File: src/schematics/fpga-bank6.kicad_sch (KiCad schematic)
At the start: 7 parts

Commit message: Updates the root page
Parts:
- renumbered C72 to C66, C73 to C67, C74 to C68, C75 to C69, C76 to C70, C77 to C71
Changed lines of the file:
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@@
 		(dnp no)
 		(fields_autoplaced yes)
-		(property "Reference" "#PWR057"
+		(property "Reference" "#PWR050"
 			(at 148.59 45.72 0)
 			(effects
@@
 		(instances
 			(project "ecap5-bsom"
-				(path "/c5fd18a3-9aa0-4151-b6e0-94da3d606686/9ec64d27-698a-408d-bb9c-7e381193a80d/95fcda06-cda0-4eca-ae7c-fe055bbdf4e0"
-					(reference "#PWR057")
+				(path "/c5fd18a3-9aa0-4151-b6e0-94da3d606686/624c8ae5-3519-4938-8e49-46a13f6c30b9"
+					(reference "#PWR050")
 					(unit 1)
 				)
@@
 		(dnp no)
 		(fields_autoplaced yes)
-		(property "Reference" "#PWR054"
+		(property "Reference" "#PWR047"
 			(at 118.11 45.72 0)
 			(effects
@@
 		(instances
 			(project "ecap5-bsom"
-				(path "/c5fd18a3-9aa0-4151-b6e0-94da3d606686/9ec64d27-698a-408d-bb9c-7e381193a80d/95fcda06-cda0-4eca-ae7c-fe055bbdf4e0"
-					(reference "#PWR054")
+				(path "/c5fd18a3-9aa0-4151-b6e0-94da3d606686/624c8ae5-3519-4938-8e49-46a13f6c30b9"
+					(reference "#PWR047")
 					(unit 1)
 				)
@@
 		(dnp no)
 		(fields_autoplaced yes)
-		(property "Reference" "C75"
+		(property "Reference" "C69"
 			(at 146.05 34.2962 0)
 			(effects
@@
 		(instances
 			(project "ecap5-bsom"
-				(path "/c5fd18a3-9aa0-4151-b6e0-94da3d606686/9ec64d27-698a-408d-bb9c-7e381193a80d/95fcda06-cda0-4eca-ae7c-fe055bbdf4e0"
-					(reference "C75")
+				(path "/c5fd18a3-9aa0-4151-b6e0-94da3d606686/624c8ae5-3519-4938-8e49-46a13f6c30b9"
+					(reference "C69")
 					(unit 1)
 				)
@@
 		(dnp no)
 		(fields_autoplaced yes)
-		(property "Reference" "#PWR053"
+		(property "Reference" "#PWR046"
 			(at 118.11 31.75 0)
 			(effects
@@
 		(instances
 			(project "ecap5-bsom"
-				(path "/c5fd18a3-9aa0-4151-b6e0-94da3d606686/9ec64d27-698a-408d-bb9c-7e381193a80d/95fcda06-cda0-4eca-ae7c-fe055bbdf4e0"
-					(reference "#PWR053")
+				(path "/c5fd18a3-9aa0-4151-b6e0-94da3d606686/624c8ae5-3519-4938-8e49-46a13f6c30b9"
+					(reference "#PWR046")
 					(unit 1)
 				)
@@
 		(dnp no)
 		(fields_autoplaced yes)
-		(property "Reference" "#PWR059"
+		(property "Reference" "#PWR052"
 			(at 170.18 45.72 0)
 			(effects
@@
 		(instances
 			(project "ecap5-bsom"
-				(path "/c5fd18a3-9aa0-4151-b6e0-94da3d606686/9ec64d27-698a-408d-bb9c-7e381193a80d/95fcda06-cda0-4eca-ae7c-fe055bbdf4e0"
-					(reference "#PWR059")
+				(path "/c5fd18a3-9aa0-4151-b6e0-94da3d606686/624c8ae5-3519-4938-8e49-46a13f6c30b9"
+					(reference "#PWR052")
 					(unit 1)
 				)
@@
 		(dnp no)
 		(fields_autoplaced yes)
-		(property "Reference" "#PWR058"
+		(property "Reference" "#PWR051"
 			(at 158.75 45.72 0)
 			(effects
@@
 		(instances
 			(project "ecap5-bsom"
-				(path "/c5fd18a3-9aa0-4151-b6e0-94da3d606686/9ec64d27-698a-408d-bb9c-7e381193a80d/95fcda06-cda0-4eca-ae7c-fe055bbdf4e0"
-					(reference "#PWR058")
+				(path "/c5fd18a3-9aa0-4151-b6e0-94da3d606686/624c8ae5-3519-4938-8e49-46a13f6c30b9"
+					(reference "#PWR051")
 					(unit 1)
 				)
@@
 		(dnp no)
 		(fields_autoplaced yes)
-		(property "Reference" "#PWR055"
+		(property "Reference" "#PWR048"
 			(at 128.27 45.72 0)
 			(effects
@@
 		(instances
 			(project "ecap5-bsom"
-				(path "/c5fd18a3-9aa0-4151-b6e0-94da3d606686/9ec64d27-698a-408d-bb9c-7e381193a80d/95fcda06-cda0-4eca-ae7c-fe055bbdf4e0"
-					(reference "#PWR055")
+				(path "/c5fd18a3-9aa0-4151-b6e0-94da3d606686/624c8ae5-3519-4938-8e49-46a13f6c30b9"
+					(reference "#PWR048")
 					(unit 1)
 				)
@@
 		(dnp no)
 		(fields_autoplaced yes)
-		(property "Reference" "C72"
+		(property "Reference" "C66"
 			(at 115.57 34.2962 0)
 			(effects
@@
 		(instances
 			(project "ecap5-bsom"
-				(path "/c5fd18a3-9aa0-4151-b6e0-94da3d606686/9ec64d27-698a-408d-bb9c-7e381193a80d/95fcda06-cda0-4eca-ae7c-fe055bbdf4e0"
-					(reference "C72")
+				(path "/c5fd18a3-9aa0-4151-b6e0-94da3d606686/624c8ae5-3519-4938-8e49-46a13f6c30b9"
+					(reference "C66")
 					(unit 1)
 				)
@@
 		(dnp no)
 		(fields_autoplaced yes)
-		(property "Reference" "C73"
+		(property "Reference" "C67"
 			(at 125.73 34.2962 0)
 			(effects
@@
 		(instances
 			(project "ecap5-bsom"
-				(path "/c5fd18a3-9aa0-4151-b6e0-94da3d606686/9ec64d27-698a-408d-bb9c-7e381193a80d/95fcda06-cda0-4eca-ae7c-fe055bbdf4e0"
-					(reference "C73")
+				(path "/c5fd18a3-9aa0-4151-b6e0-94da3d606686/624c8ae5-3519-4938-8e49-46a13f6c30b9"
+					(reference "C67")
 					(unit 1)
 				)
@@
 		(dnp no)
 		(fields_autoplaced yes)
-		(property "Reference" "C76"
+		(property "Reference" "C70"
 			(at 156.21 34.2962 0)
 			(effects
@@
 		(instances
 			(project "ecap5-bsom"
-				(path "/c5fd18a3-9aa0-4151-b6e0-94da3d606686/9ec64d27-698a-408d-bb9c-7e381193a80d/95fcda06-cda0-4eca-ae7c-fe055bbdf4e0"
-					(reference "C76")
+				(path "/c5fd18a3-9aa0-4151-b6e0-94da3d606686/624c8ae5-3519-4938-8e49-46a13f6c30b9"
+					(reference "C70")
 					(unit 1)
 				)
@@
 		(dnp no)
 		(fields_autoplaced yes)
-		(property "Reference" "C74"
+		(property "Reference" "C68"
 			(at 135.89 34.2962 0)
 			(effects
@@
 		(instances
 			(project "ecap5-bsom"
-				(path "/c5fd18a3-9aa0-4151-b6e0-94da3d606686/9ec64d27-698a-408d-bb9c-7e381193a80d/95fcda06-cda0-4eca-ae7c-fe055bbdf4e0"
-					(reference "C74")
+				(path "/c5fd18a3-9aa0-4151-b6e0-94da3d606686/624c8ae5-3519-4938-8e49-46a13f6c30b9"
+					(reference "C68")
 					(unit 1)
 				)
@@
 		(dnp no)
 		(fields_autoplaced yes)
-		(property "Reference" "#PWR056"
+		(property "Reference" "#PWR049"
 			(at 138.43 45.72 0)
 			(effects
@@
 		(instances
 			(project "ecap5-bsom"
-				(path "/c5fd18a3-9aa0-4151-b6e0-94da3d606686/9ec64d27-698a-408d-bb9c-7e381193a80d/95fcda06-cda0-4eca-ae7c-fe055bbdf4e0"
-					(reference "#PWR056")
+				(path "/c5fd18a3-9aa0-4151-b6e0-94da3d606686/624c8ae5-3519-4938-8e49-46a13f6c30b9"
+					(reference "#PWR049")
 					(unit 1)
 				)
@@
 		(dnp no)
 		(fields_autoplaced yes)
-		(property "Reference" "C77"
+		(property "Reference" "C71"
 			(at 167.64 34.2962 0)
 			(effects
@@
 		(instances
 			(project "ecap5-bsom"
-				(path "/c5fd18a3-9aa0-4151-b6e0-94da3d606686/9ec64d27-698a-408d-bb9c-7e381193a80d/95fcda06-cda0-4eca-ae7c-fe055bbdf4e0"
-					(reference "C77")
+				(path "/c5fd18a3-9aa0-4151-b6e0-94da3d606686/624c8ae5-3519-4938-8e49-46a13f6c30b9"
+					(reference "C71")
 					(unit 1)
 				)
@@
 		(instances
 			(project "ecap5-bsom"
-				(path "/c5fd18a3-9aa0-4151-b6e0-94da3d606686/9ec64d27-698a-408d-bb9c-7e381193a80d/95fcda06-cda0-4eca-ae7c-fe055bbdf4e0"
+				(path "/c5fd18a3-9aa0-4151-b6e0-94da3d606686/624c8ae5-3519-4938-8e49-46a13f6c30b9"
 					(reference "U6")
 					(unit 7)

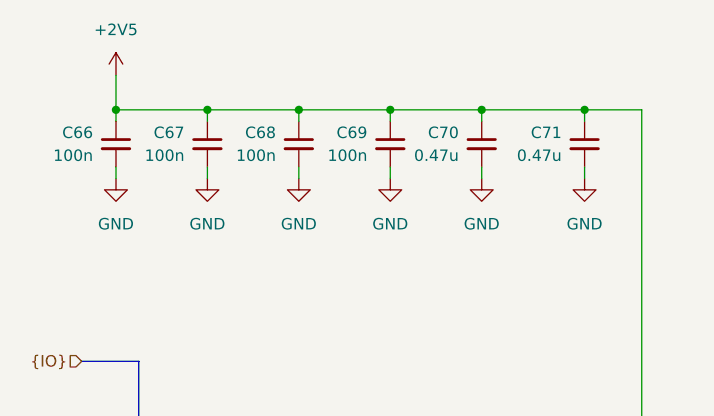
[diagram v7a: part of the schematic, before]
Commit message: Fixes ERC issues
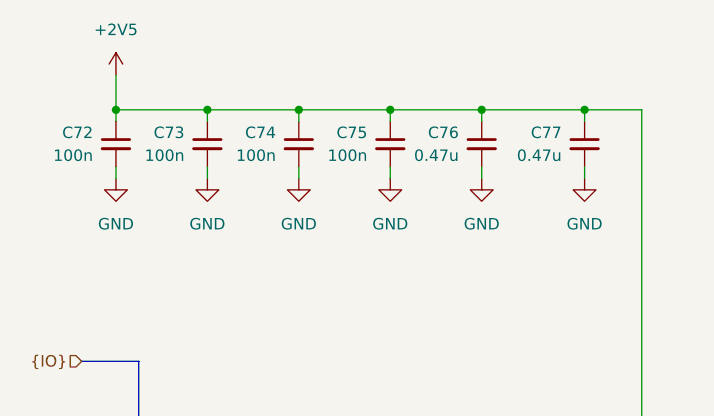
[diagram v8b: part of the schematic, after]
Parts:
- renumbered C66 to C72, C67 to C73, C68 to C74, C69 to C75, C70 to C76, C71 to C77
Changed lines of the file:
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@@
 		(dnp no)
 		(fields_autoplaced yes)
-		(property "Reference" "#PWR050"
+		(property "Reference" "#PWR058"
 			(at 148.59 45.72 0)
 			(effects
@@
 			(project "ecap5-bsom"
 				(path "/c5fd18a3-9aa0-4151-b6e0-94da3d606686/624c8ae5-3519-4938-8e49-46a13f6c30b9"
-					(reference "#PWR050")
+					(reference "#PWR058")
 					(unit 1)
 				)
@@
 		(dnp no)
 		(fields_autoplaced yes)
-		(property "Reference" "#PWR047"
+		(property "Reference" "#PWR055"
 			(at 118.11 45.72 0)
 			(effects
@@
 			(project "ecap5-bsom"
 				(path "/c5fd18a3-9aa0-4151-b6e0-94da3d606686/624c8ae5-3519-4938-8e49-46a13f6c30b9"
-					(reference "#PWR047")
+					(reference "#PWR055")
 					(unit 1)
 				)
@@
 		(dnp no)
 		(fields_autoplaced yes)
-		(property "Reference" "C69"
+		(property "Reference" "C75"
 			(at 146.05 34.2962 0)
 			(effects
@@
 			(project "ecap5-bsom"
 				(path "/c5fd18a3-9aa0-4151-b6e0-94da3d606686/624c8ae5-3519-4938-8e49-46a13f6c30b9"
-					(reference "C69")
+					(reference "C75")
 					(unit 1)
 				)
@@
 		(dnp no)
 		(fields_autoplaced yes)
-		(property "Reference" "#PWR046"
+		(property "Reference" "#PWR054"
 			(at 118.11 31.75 0)
 			(effects
@@
 			(project "ecap5-bsom"
 				(path "/c5fd18a3-9aa0-4151-b6e0-94da3d606686/624c8ae5-3519-4938-8e49-46a13f6c30b9"
-					(reference "#PWR046")
+					(reference "#PWR054")
 					(unit 1)
 				)
@@
 		(dnp no)
 		(fields_autoplaced yes)
-		(property "Reference" "#PWR052"
+		(property "Reference" "#PWR060"
 			(at 170.18 45.72 0)
 			(effects
@@
 			(project "ecap5-bsom"
 				(path "/c5fd18a3-9aa0-4151-b6e0-94da3d606686/624c8ae5-3519-4938-8e49-46a13f6c30b9"
-					(reference "#PWR052")
+					(reference "#PWR060")
 					(unit 1)
 				)
@@
 		(dnp no)
 		(fields_autoplaced yes)
-		(property "Reference" "#PWR051"
+		(property "Reference" "#PWR059"
 			(at 158.75 45.72 0)
 			(effects
@@
 			(project "ecap5-bsom"
 				(path "/c5fd18a3-9aa0-4151-b6e0-94da3d606686/624c8ae5-3519-4938-8e49-46a13f6c30b9"
-					(reference "#PWR051")
+					(reference "#PWR059")
 					(unit 1)
 				)
@@
 		(dnp no)
 		(fields_autoplaced yes)
-		(property "Reference" "#PWR048"
+		(property "Reference" "#PWR056"
 			(at 128.27 45.72 0)
 			(effects
@@
 			(project "ecap5-bsom"
 				(path "/c5fd18a3-9aa0-4151-b6e0-94da3d606686/624c8ae5-3519-4938-8e49-46a13f6c30b9"
-					(reference "#PWR048")
+					(reference "#PWR056")
 					(unit 1)
 				)
@@
 		(dnp no)
 		(fields_autoplaced yes)
-		(property "Reference" "C66"
+		(property "Reference" "C72"
 			(at 115.57 34.2962 0)
 			(effects
@@
 			(project "ecap5-bsom"
 				(path "/c5fd18a3-9aa0-4151-b6e0-94da3d606686/624c8ae5-3519-4938-8e49-46a13f6c30b9"
-					(reference "C66")
+					(reference "C72")
 					(unit 1)
 				)
@@
 		(dnp no)
 		(fields_autoplaced yes)
-		(property "Reference" "C67"
+		(property "Reference" "C73"
 			(at 125.73 34.2962 0)
 			(effects
@@
 			(project "ecap5-bsom"
 				(path "/c5fd18a3-9aa0-4151-b6e0-94da3d606686/624c8ae5-3519-4938-8e49-46a13f6c30b9"
-					(reference "C67")
+					(reference "C73")
 					(unit 1)
 				)
@@
 		(dnp no)
 		(fields_autoplaced yes)
-		(property "Reference" "C70"
+		(property "Reference" "C76"
 			(at 156.21 34.2962 0)
 			(effects
@@
 			(project "ecap5-bsom"
 				(path "/c5fd18a3-9aa0-4151-b6e0-94da3d606686/624c8ae5-3519-4938-8e49-46a13f6c30b9"
-					(reference "C70")
+					(reference "C76")
 					(unit 1)
 				)
@@
 		(dnp no)
 		(fields_autoplaced yes)
-		(property "Reference" "C68"
+		(property "Reference" "C74"
 			(at 135.89 34.2962 0)
 			(effects
@@
 			(project "ecap5-bsom"
 				(path "/c5fd18a3-9aa0-4151-b6e0-94da3d606686/624c8ae5-3519-4938-8e49-46a13f6c30b9"
-					(reference "C68")
+					(reference "C74")
 					(unit 1)
 				)
@@
 		(dnp no)
 		(fields_autoplaced yes)
-		(property "Reference" "#PWR049"
+		(property "Reference" "#PWR057"
 			(at 138.43 45.72 0)
 			(effects
@@
 			(project "ecap5-bsom"
 				(path "/c5fd18a3-9aa0-4151-b6e0-94da3d606686/624c8ae5-3519-4938-8e49-46a13f6c30b9"
-					(reference "#PWR049")
+					(reference "#PWR057")
 					(unit 1)
 				)
@@
 		(dnp no)
 		(fields_autoplaced yes)
-		(property "Reference" "C71"
+		(property "Reference" "C77"
 			(at 167.64 34.2962 0)
 			(effects
@@
 			(project "ecap5-bsom"
 				(path "/c5fd18a3-9aa0-4151-b6e0-94da3d606686/624c8ae5-3519-4938-8e49-46a13f6c30b9"
-					(reference "C71")
-					(unit 1)
-				)
+					(reference "C77")
+					(unit 1)
+				)
